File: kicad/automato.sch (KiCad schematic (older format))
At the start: 80 parts, among them J1 USB_C_Receptacle, J10 QWIIC 0, J12 STEMMA 0, J2 LiPo, J4 Screw_Terminal_01x14, J5 USB_C_Receptacle, J6 Conn_Coaxial, J7 1-WIRE, J8 Micro_SD_Card_Det, J9 UART2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

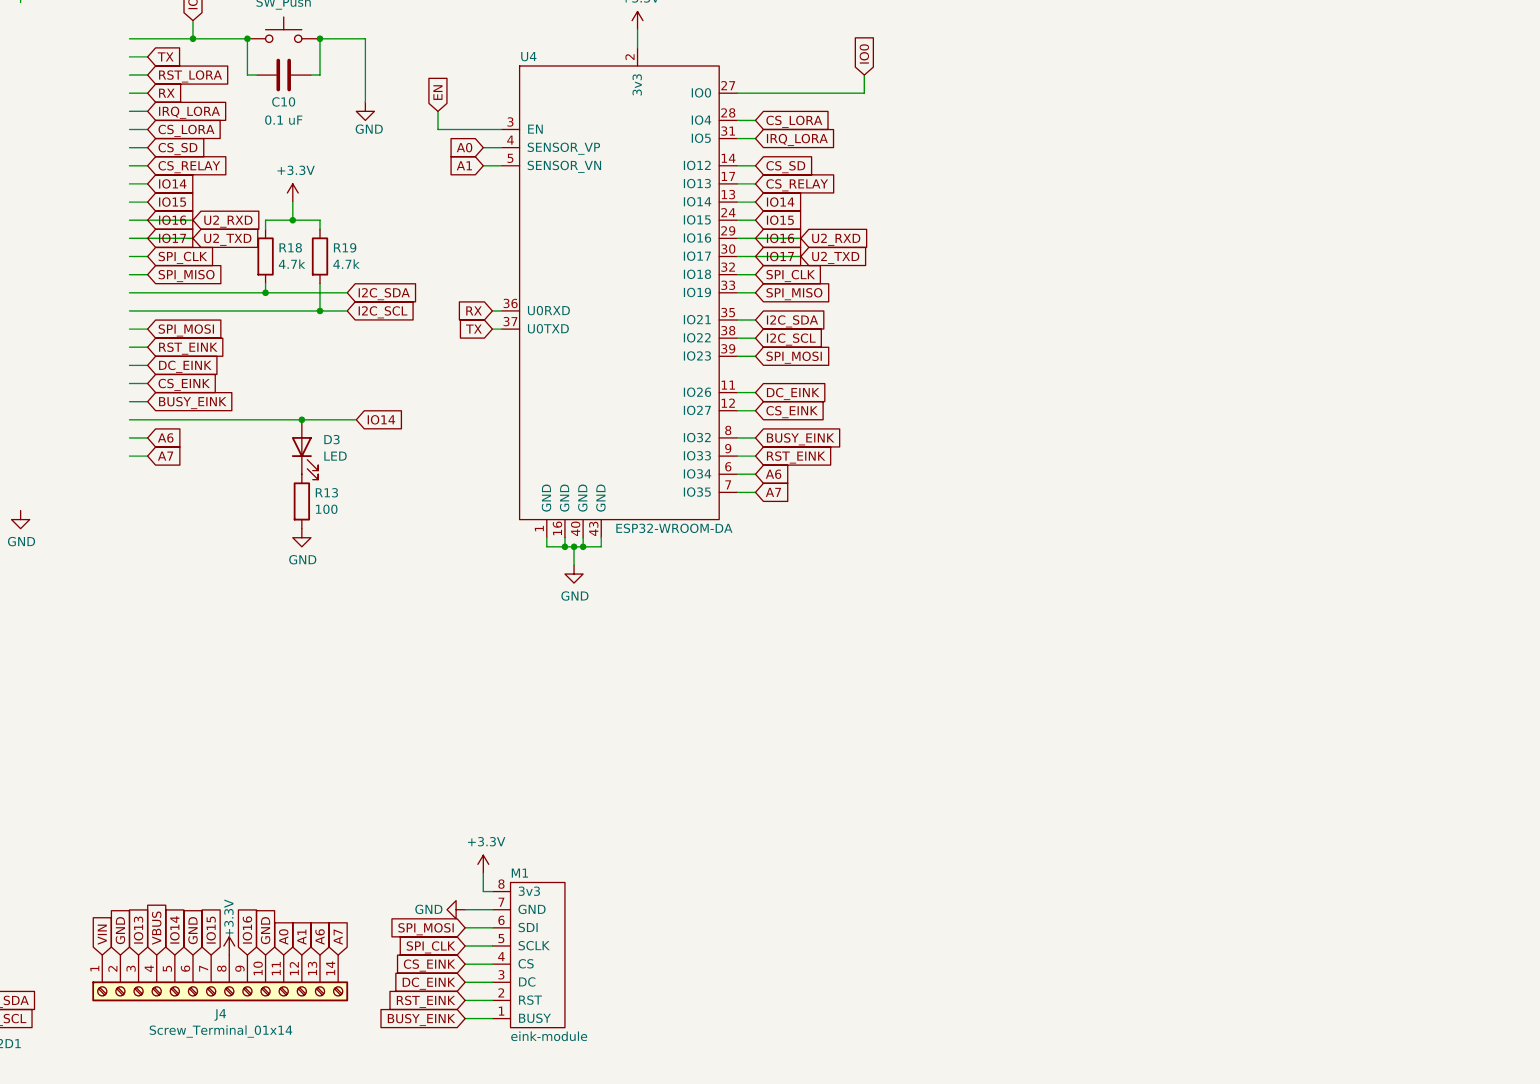
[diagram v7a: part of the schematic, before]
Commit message: add mounting hole pads
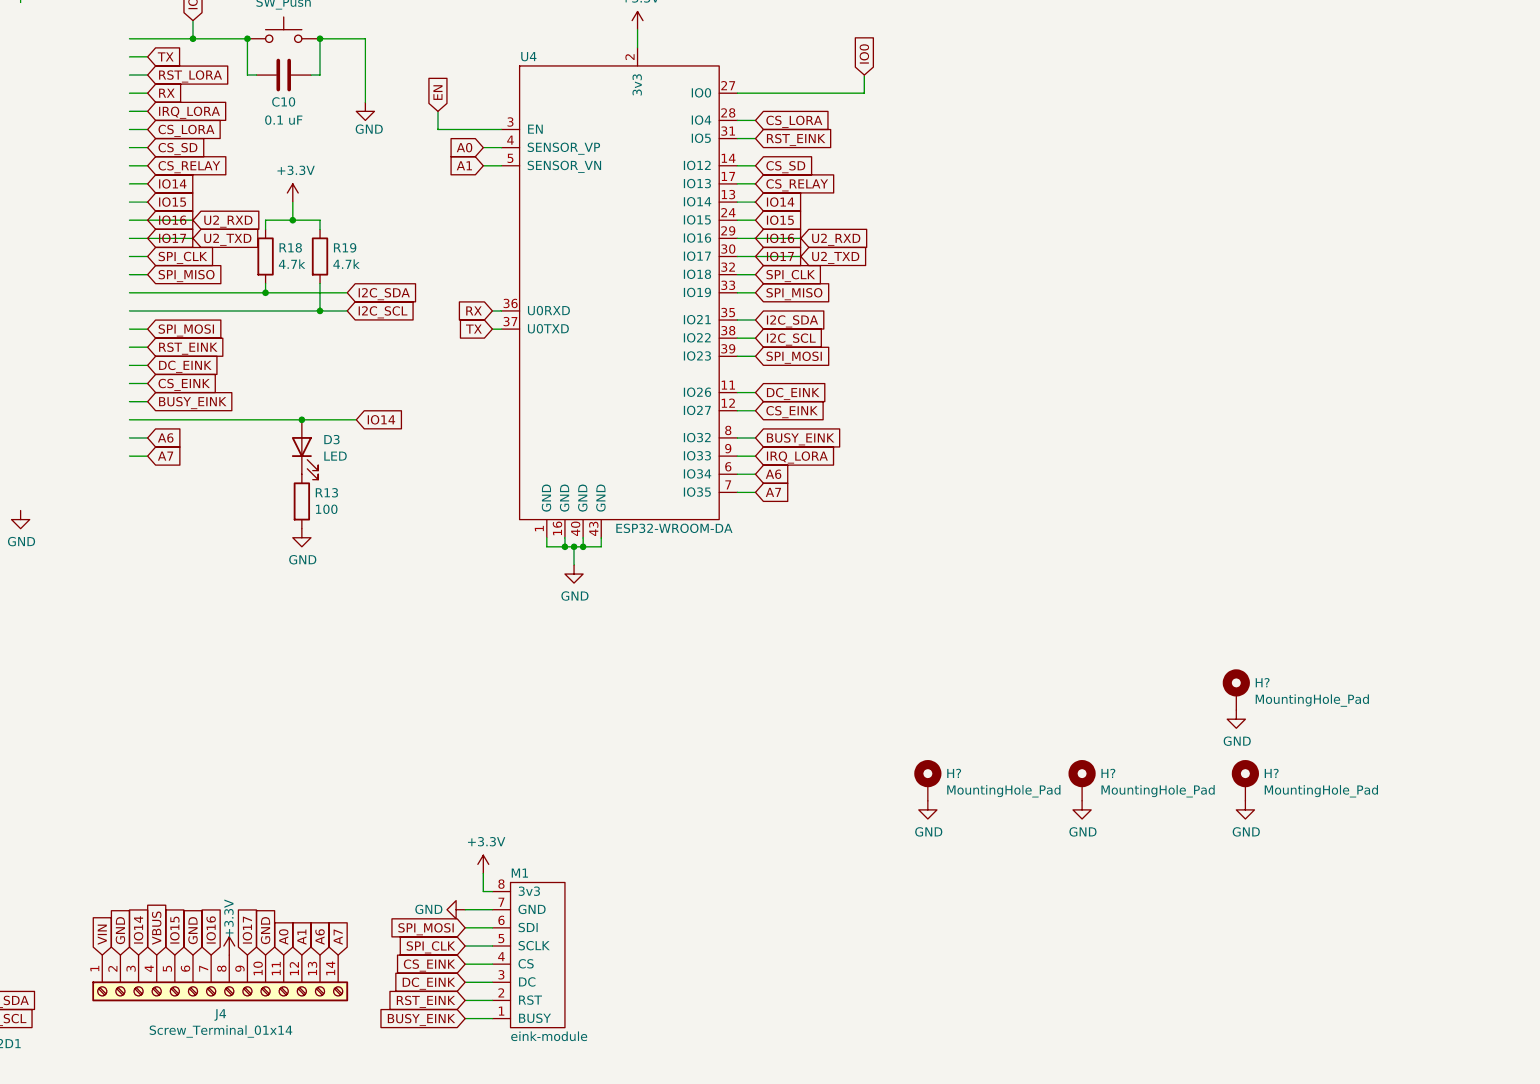
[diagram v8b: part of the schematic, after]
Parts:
- added H? (x4): MountingHole_Pad, MountingHole:MountingHole_3.2mm_M3_Pad_TopBottom, symbol Mechanical:MountingHole_Pad
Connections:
- net labels removed: IO13
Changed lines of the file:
@@
 Wire Wire Line
 	9550 6750 9650 6750
-Text GLabel 10200 9800 1    50   Input ~ 0
+Text GLabel 10000 9800 1    50   Input ~ 0
 IO16
 Text GLabel 9600 9800 1    50   Input ~ 0
-IO13
+IO14
 Text GLabel 9800 9800 1    50   Input ~ 0
-IO14
-Text GLabel 10000 9800 1    50   Input ~ 0
 IO15
 $Comp
@@
 Text GLabel 13000 6800 2    50   Input ~ 0
 CS_EINK
-Text GLabel 13000 7050 2    50   Input ~ 0
+Text GLabel 13000 5300 2    50   Input ~ 0
 RST_EINK
 Wire Wire Line
@@
 Text GLabel 13000 5200 2    50   Input ~ 0
 CS_LORA
-Text GLabel 13000 5300 2    50   Input ~ 0
+Text GLabel 13000 7050 2    50   Input ~ 0
 IRQ_LORA
 Wire Wire Line
@@
 Wire Wire Line
 	12900 5950 13250 5950
+Text GLabel 10200 9800 1    50   Input ~ 0
+IO17
+$Comp
+L Mechanical:MountingHole_Pad H?
+U 1 1 63315064
+P 15700 8850
+F 0 "H?" H 15800 8899 50  0000 L CNN
+F 1 "MountingHole_Pad" H 15800 8808 50  0000 L CNN
+F 2 "MountingHole:MountingHole_3.2mm_M3_Pad_TopBottom" H 15700 8850 50  0001 C CNN
+F 3 "~" H 15700 8850 50  0001 C CNN
+	1    15700 8850
+	1    0    0    -1
+$EndComp
+$Comp
+L power:GND #PWR?
+U 1 1 63315EC1
+P 15700 8950
+F 0 "#PWR?" H 15700 8700 50  0001 C CNN
+F 1 "GND" H 15705 8777 50  0000 C CNN
+F 2 "" H 15700 8950 50  0001 C CNN
+F 3 "" H 15700 8950 50  0001 C CNN
+	1    15700 8950
+	1    0    0    -1
+$EndComp
+$Comp
+L Mechanical:MountingHole_Pad H?
+U 1 1 63316F8B
+P 14800 8850
+F 0 "H?" H 14900 8899 50  0000 L CNN
+F 1 "MountingHole_Pad" H 14900 8808 50  0000 L CNN
+F 2 "MountingHole:MountingHole_3.2mm_M3_Pad_TopBottom" H 14800 8850 50  0001 C CNN
+F 3 "~" H 14800 8850 50  0001 C CNN
+	1    14800 8850
+	1    0    0    -1
+$EndComp
+$Comp
+L power:GND #PWR?
+U 1 1 63316F91
+P 14800 8950
+F 0 "#PWR?" H 14800 8700 50  0001 C CNN
+F 1 "GND" H 14805 8777 50  0000 C CNN
+F 2 "" H 14800 8950 50  0001 C CNN
+F 3 "" H 14800 8950 50  0001 C CNN
+	1    14800 8950
+	1    0    0    -1
+$EndComp
+$Comp
+L Mechanical:MountingHole_Pad H?
+U 1 1 63338870
+P 13950 8850
+F 0 "H?" H 14050 8899 50  0000 L CNN
+F 1 "MountingHole_Pad" H 14050 8808 50  0000 L CNN
+F 2 "MountingHole:MountingHole_3.2mm_M3_Pad_TopBottom" H 13950 8850 50  0001 C CNN
+F 3 "~" H 13950 8850 50  0001 C CNN
+	1    13950 8850
+	1    0    0    -1
+$EndComp
+$Comp
+L power:GND #PWR?
+U 1 1 63338876
+P 13950 8950
+F 0 "#PWR?" H 13950 8700 50  0001 C CNN
+F 1 "GND" H 13955 8777 50  0000 C CNN
+F 2 "" H 13950 8950 50  0001 C CNN
+F 3 "" H 13950 8950 50  0001 C CNN
+	1    13950 8950
+	1    0    0    -1
+$EndComp
+$Comp
+L Mechanical:MountingHole_Pad H?
+U 1 1 63359F55
+P 15650 8350
+F 0 "H?" H 15750 8399 50  0000 L CNN
+F 1 "MountingHole_Pad" H 15750 8308 50  0000 L CNN
+F 2 "MountingHole:MountingHole_3.2mm_M3_Pad_TopBottom" H 15650 8350 50  0001 C CNN
+F 3 "~" H 15650 8350 50  0001 C CNN
+	1    15650 8350
+	1    0    0    -1
+$EndComp
+$Comp
+L power:GND #PWR?
+U 1 1 63359F5B
+P 15650 8450
+F 0 "#PWR?" H 15650 8200 50  0001 C CNN
+F 1 "GND" H 15655 8277 50  0000 C CNN
+F 2 "" H 15650 8450 50  0001 C CNN
+F 3 "" H 15650 8450 50  0001 C CNN
+	1    15650 8450
+	1    0    0    -1
+$EndComp
 $EndSCHEMATC
